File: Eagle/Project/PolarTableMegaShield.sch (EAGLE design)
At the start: 41 parts, among them IC2 LM358D, J10 LED + Radio, J3 Pi Connection, J5 IR Sensors, J6 Switch A + B, J7 Switch C + D, J8 Switch E + F, Q1 BC337, Q2 2N3906, Q3 2N3904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

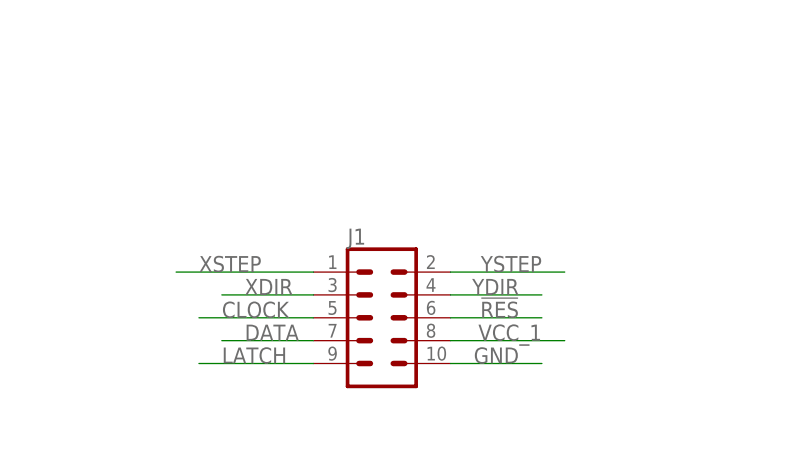
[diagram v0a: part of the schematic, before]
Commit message: Changed the connector to be 6x2 so the shift reg could run at 3.3V
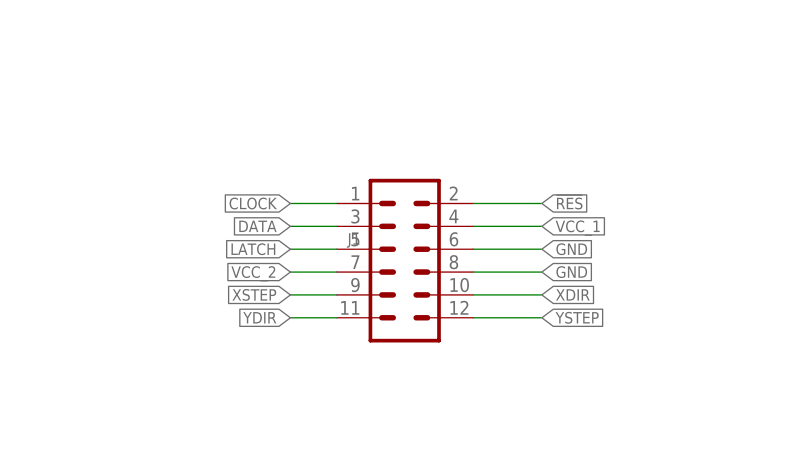
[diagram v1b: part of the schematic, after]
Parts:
- J1: device SparkFun-Connectors:CONN_05X2RA -> keir_library:CONN_06X21.24MM_RA_MALE
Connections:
- net !RES: now also J1.2; no longer J1.6
- net CLOCK: now also J1.1; no longer J1.5
- net DATA: now also J1.3; no longer J1.7
- net GND: now also J1.6, J1.8; no longer J1.10
- net LATCH: now also J1.5; no longer J1.9
- net VCC_1: now also J1.4; no longer J1.8
- net VCC_2: now also J1.7
- net XDIR: now also J1.10; no longer J1.3
- net XSTEP: now also J1.9; no longer J1.1
- net YDIR: now also J1.11; no longer J1.4
- net YSTEP: now also J1.12; no longer J1.2
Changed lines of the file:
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@@
 <part name="P+3" library="SparkFun-PowerSymbols" library_urn="urn:adsk.eagle:library:530" deviceset="VCC_1" device="" value="5V"/>
 <part name="GND1" library="SparkFun" deviceset="GND" device=""/>
-<part name="J1" library="SparkFun-Connectors" library_urn="urn:adsk.eagle:library:513" deviceset="CONN_05X2" device="RA" package3d_urn="urn:adsk.eagle:package:38115/1"/>
+<part name="J1" library="keir_library" deviceset="CONN_06X2" device="1.24MM_RA_MALE" package3d_urn="urn:adsk.eagle:package:38277/1"/>
 <part name="SUPPLY4" library="SparkFun-PowerSymbols" library_urn="urn:adsk.eagle:library:530" deviceset="VCC_2" device="" value="3.3V"/>
 </parts>
@@
 <instance part="J1" gate="G$1" x="66.04" y="20.32" smashed="yes">
 <attribute name="VALUE" x="62.23" y="10.414" size="1.778" layer="96" font="vector"/>
-<attribute name="NAME" x="62.23" y="28.448" size="1.778" layer="95" font="vector"/>
+<attribute name="NAME" x="62.23" y="28.448" size="1.27" layer="95" font="vector"/>
 </instance>
 <instance part="SUPPLY4" gate="G$1" x="30.48" y="233.68" smashed="yes">
@@
 </segment>
 <segment>
-<pinref part="J1" gate="G$1" pin="10"/>
-<wire x1="73.66" y1="15.24" x2="83.82" y2="15.24" width="0.1524" layer="91"/>
-<label x="81.28" y="15.24" size="1.778" layer="95" align="bottom-right"/>
+<pinref part="J1" gate="G$1" pin="8"/>
+<wire x1="76.2" y1="25.4" x2="83.82" y2="25.4" width="0.1524" layer="91"/>
+<label x="83.82" y="25.4" size="1.27" layer="95" xref="yes"/>
+</segment>
+<segment>
+<pinref part="J1" gate="G$1" pin="6"/>
+<wire x1="76.2" y1="27.94" x2="83.82" y2="27.94" width="0.1524" layer="91"/>
+<label x="83.82" y="27.94" size="1.27" layer="95" xref="yes"/>
 </segment>
 </net>
@@
 </segment>
 <segment>
-<pinref part="J1" gate="G$1" pin="6"/>
-<wire x1="73.66" y1="20.32" x2="83.82" y2="20.32" width="0.1524" layer="91"/>
-<label x="81.28" y="20.32" size="1.778" layer="95" align="bottom-right"/>
+<pinref part="J1" gate="G$1" pin="2"/>
+<wire x1="76.2" y1="33.02" x2="83.82" y2="33.02" width="0.1524" layer="91"/>
+<label x="83.82" y="33.02" size="1.27" layer="95" xref="yes"/>
 </segment>
 </net>
@@
 </segment>
 <segment>
-<pinref part="J1" gate="G$1" pin="3"/>
-<wire x1="58.42" y1="22.86" x2="48.26" y2="22.86" width="0.1524" layer="91"/>
-<label x="50.8" y="22.86" size="1.778" layer="95"/>
+<pinref part="J1" gate="G$1" pin="10"/>
+<wire x1="76.2" y1="22.86" x2="83.82" y2="22.86" width="0.1524" layer="91"/>
+<label x="83.82" y="22.86" size="1.27" layer="95" xref="yes"/>
 </segment>
 </net>
@@
 </segment>
 <segment>
-<pinref part="J1" gate="G$1" pin="1"/>
-<wire x1="58.42" y1="25.4" x2="43.18" y2="25.4" width="0.1524" layer="91"/>
-<label x="45.72" y="25.4" size="1.778" layer="95"/>
+<pinref part="J1" gate="G$1" pin="9"/>
+<wire x1="60.96" y1="22.86" x2="55.88" y2="22.86" width="0.1524" layer="91"/>
+<label x="55.88" y="22.86" size="1.27" layer="95" rot="R180" xref="yes"/>
 </segment>
 </net>
@@
 </segment>
 <segment>
-<pinref part="J1" gate="G$1" pin="2"/>
-<wire x1="73.66" y1="25.4" x2="86.36" y2="25.4" width="0.1524" layer="91"/>
-<label x="83.82" y="25.4" size="1.778" layer="95" align="bottom-right"/>
+<pinref part="J1" gate="G$1" pin="12"/>
+<wire x1="76.2" y1="20.32" x2="83.82" y2="20.32" width="0.1524" layer="91"/>
+<label x="83.82" y="20.32" size="1.27" layer="95" xref="yes"/>
 </segment>
 </net>
@@
 </segment>
 <segment>
-<pinref part="J1" gate="G$1" pin="4"/>
-<wire x1="73.66" y1="22.86" x2="83.82" y2="22.86" width="0.1524" layer="91"/>
-<label x="81.28" y="22.86" size="1.778" layer="95" align="bottom-right"/>
+<pinref part="J1" gate="G$1" pin="11"/>
+<wire x1="60.96" y1="20.32" x2="55.88" y2="20.32" width="0.1524" layer="91"/>
+<label x="55.88" y="20.32" size="1.27" layer="95" rot="R180" xref="yes"/>
 </segment>
 </net>
@@
 </segment>
 <segment>
-<pinref part="J1" gate="G$1" pin="9"/>
-<wire x1="58.42" y1="15.24" x2="45.72" y2="15.24" width="0.1524" layer="91"/>
-<label x="48.26" y="15.24" size="1.778" layer="95"/>
+<pinref part="J1" gate="G$1" pin="5"/>
+<wire x1="60.96" y1="27.94" x2="55.88" y2="27.94" width="0.1524" layer="91"/>
+<label x="55.88" y="27.94" size="1.27" layer="95" rot="R180" xref="yes"/>
 </segment>
 </net>
@@
 </segment>
 <segment>
-<pinref part="J1" gate="G$1" pin="7"/>
-<wire x1="58.42" y1="17.78" x2="48.26" y2="17.78" width="0.1524" layer="91"/>
-<label x="50.8" y="17.78" size="1.778" layer="95"/>
+<pinref part="J1" gate="G$1" pin="3"/>
+<wire x1="60.96" y1="30.48" x2="55.88" y2="30.48" width="0.1524" layer="91"/>
+<label x="55.88" y="30.48" size="1.27" layer="95" rot="R180" xref="yes"/>
 </segment>
 </net>
@@
 </segment>
 <segment>
-<pinref part="J1" gate="G$1" pin="8"/>
-<wire x1="73.66" y1="17.78" x2="86.36" y2="17.78" width="0.1524" layer="91"/>
-<label x="83.82" y="17.78" size="1.778" layer="95" align="bottom-right"/>
+<pinref part="J1" gate="G$1" pin="4"/>
+<wire x1="76.2" y1="30.48" x2="83.82" y2="30.48" width="0.1524" layer="91"/>
+<label x="83.82" y="30.48" size="1.27" layer="95" xref="yes"/>
 </segment>
 </net>
@@
 <pinref part="SUPPLY4" gate="G$1" pin="VCC_2"/>
 </segment>
+<segment>
+<pinref part="J1" gate="G$1" pin="7"/>
+<wire x1="60.96" y1="25.4" x2="55.88" y2="25.4" width="0.1524" layer="91"/>
+<label x="55.88" y="25.4" size="1.27" layer="95" rot="R180" xref="yes"/>
+</segment>
 </net>
 <net name="WAKE_SW_BUF" class="4">
@@
 </segment>
 <segment>
-<pinref part="J1" gate="G$1" pin="5"/>
-<wire x1="58.42" y1="20.32" x2="45.72" y2="20.32" width="0.1524" layer="91"/>
-<label x="48.26" y="20.32" size="1.778" layer="95"/>
-</segment>
-</net>
+<pinref part="J1" gate="G$1" pin="1"/>
+<wire x1="60.96" y1="33.02" x2="55.88" y2="33.02" width="0.1524" layer="91"/>
+<label x="55.88" y="33.02" size="1.27" layer="95" rot="R180" xref="yes"/>
+</segment>
+</net>
